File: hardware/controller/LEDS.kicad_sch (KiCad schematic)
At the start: 19 parts, among them IC901 PCA9685PW_Q900,118, Q901 IRLML6402TRPBF, Q902 IRLML6402TRPBF

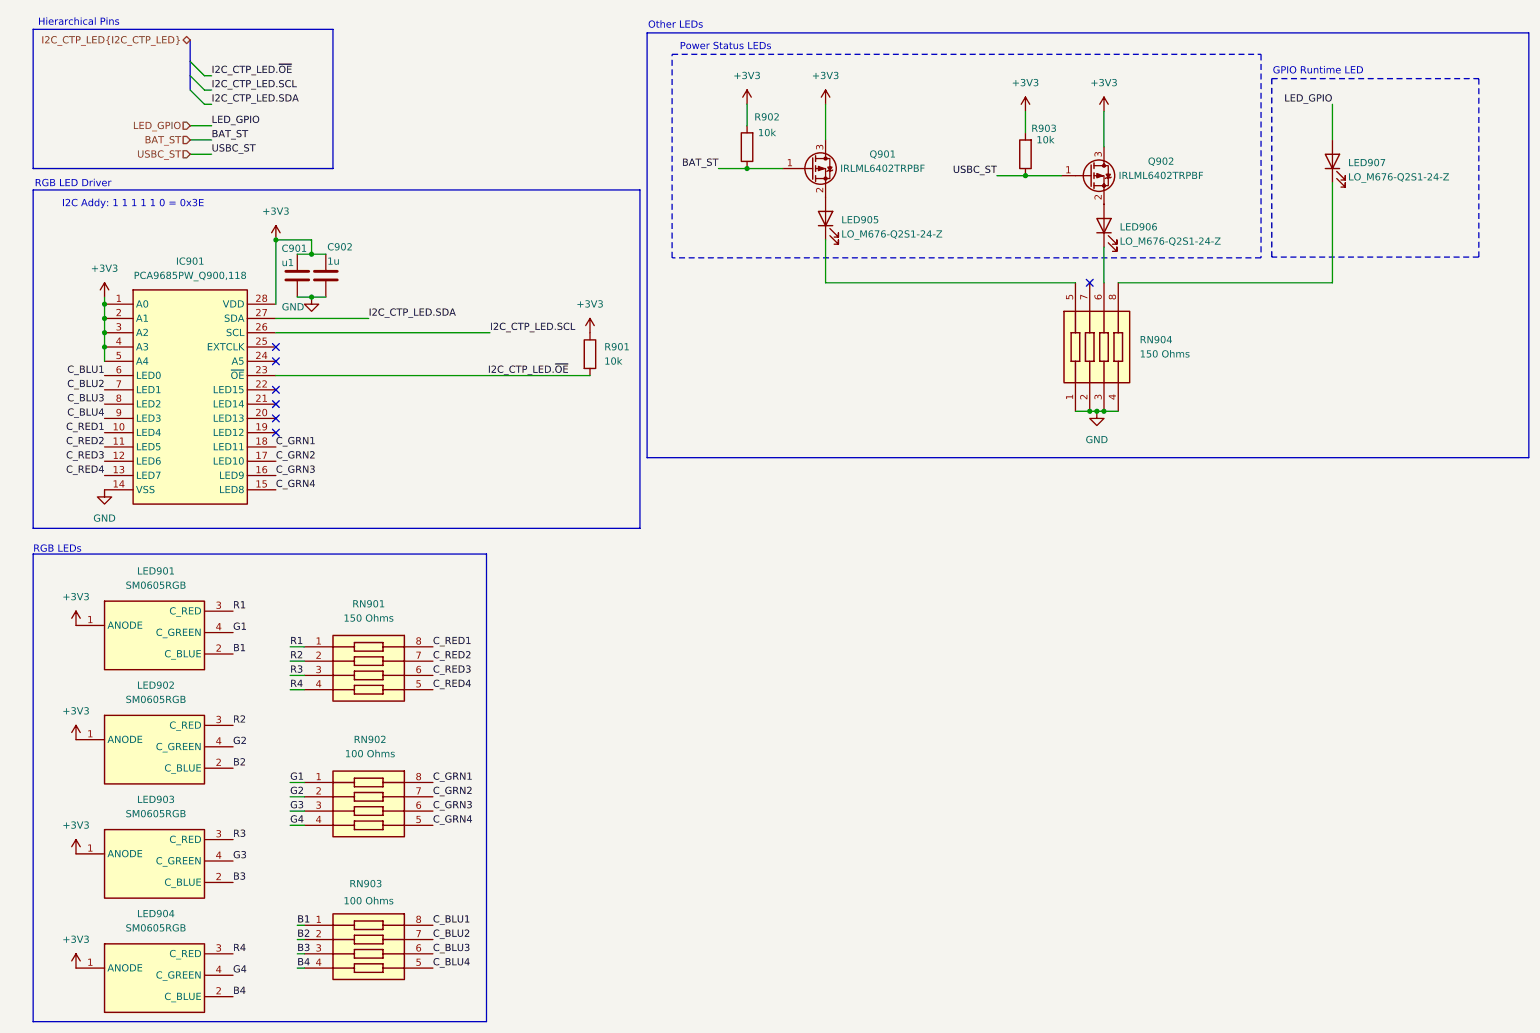
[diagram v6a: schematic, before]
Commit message: save before axing motor driver ic's
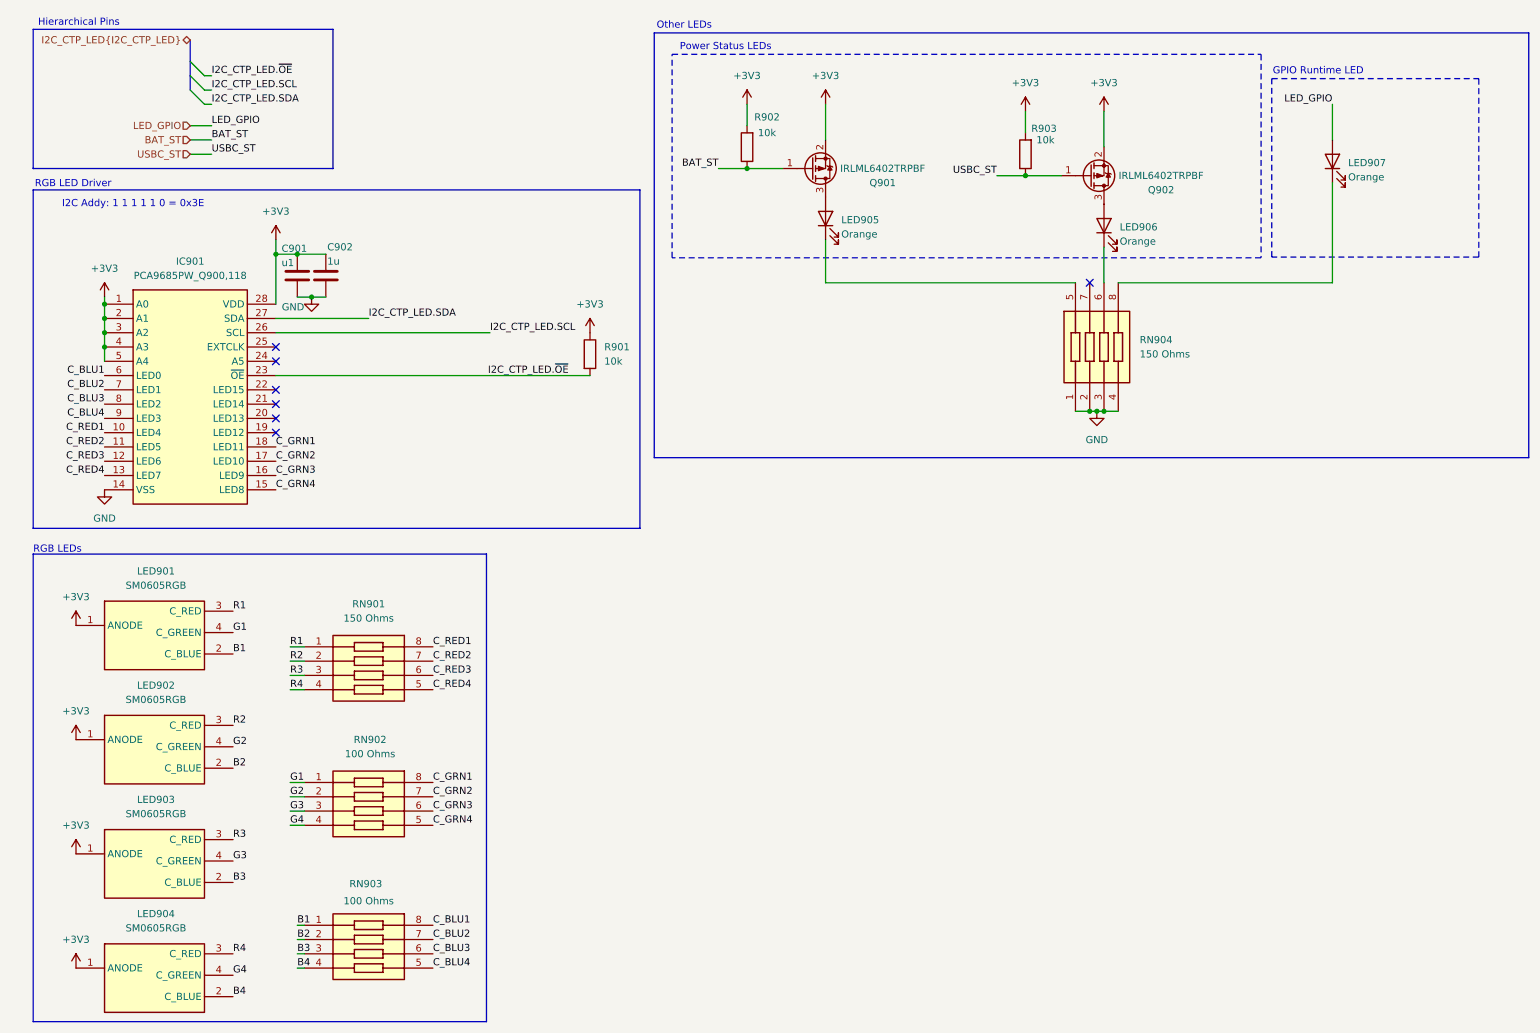
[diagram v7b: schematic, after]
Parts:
- LED905, LED906, LED907: value LO_M676-Q2S1-24-Z -> Orange
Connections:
- net +3V3: now also Q901.2 (S), Q902.2 (S); no longer Q901.3 (D), Q902.3 (D)
- net at LED906.2 (A): now also Q902.3 (D); no longer Q902.2 (S)
- net at LED905.2 (A): now also Q901.3 (D); no longer Q901.2 (S)
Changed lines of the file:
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@@
 	(paper "A4")
 	(rectangle
-		(start 124.46 17.78)
+		(start 125.73 17.78)
 		(end 281.305 93.345)
 		(stroke
@@
 	(text "Other LEDs"
 		(exclude_from_sim no)
-		(at 129.54 16.51 0)
+		(at 131.064 16.51 0)
 		(effects
 			(font
@@
 	)
 	(junction
-		(at 58.42 54.61)
+		(at 62.23 57.15)
 		(diameter 0)
 		(color 0 0 0 0)
@@
 	)
 	(junction
-		(at 64.77 57.15)
+		(at 142.24 41.91)
 		(diameter 0)
 		(color 0 0 0 0)
 	)
 	(junction
-		(at 142.24 41.91)
+		(at 27.94 66.04)
 		(diameter 0)
 		(color 0 0 0 0)
 	)
 	(junction
-		(at 27.94 66.04)
+		(at 58.42 57.15)
 		(diameter 0)
 		(color 0 0 0 0)
@@
 	(wire
 		(pts
+			(xy 58.42 57.15) (xy 58.42 66.04)
+		)
+		(stroke
+			(width 0)
+			(type default)
+		)
+	)
+	(wire
+		(pts
 			(xy 191.77 31.75) (xy 191.77 35.56)
 		)
@@
 	(wire
 		(pts
-			(xy 58.42 54.61) (xy 58.42 66.04)
+			(xy 58.42 54.61) (xy 58.42 57.15)
 		)
 		(stroke
@@
 	(wire
 		(pts
-			(xy 58.42 54.61) (xy 64.77 54.61)
+			(xy 58.42 57.15) (xy 62.23 57.15)
 		)
 		(stroke
@@
 	(wire
 		(pts
-			(xy 62.23 57.15) (xy 64.77 57.15)
-		)
-		(stroke
-			(width 0)
-			(type default)
-		)
-	)
-	(wire
-		(pts
-			(xy 64.77 57.15) (xy 67.31 57.15)
+			(xy 62.23 57.15) (xy 67.31 57.15)
 		)
 		(stroke
@@
 	(wire
 		(pts
-			(xy 64.77 54.61) (xy 64.77 57.15)
-		)
-		(stroke
-			(width 0)
-			(type default)
-		)
-	)
-	(wire
-		(pts
 			(xy 45.72 27.94) (xy 46.99 27.94)
 		)
@@
 		(lib_id "Transistor_FET:IRLML6402")
 		(at 203.2 43.18 0)
+		(mirror x)
 		(unit 1)
 		(exclude_from_sim no)
@@
 		(dnp no)
 		(property "Reference" "Q902"
-			(at 215.9 40.64 0)
+			(at 215.9 45.72 0)
 			(effects
 				(font
@@
 		)
 		(property "Footprint" "Package_TO_SOT_SMD:SOT-23"
-			(at 208.28 45.085 0)
+			(at 208.28 41.275 0)
 			(effects
 				(font
@@
 		)
 		(property "Datasheet" "https://www.infineon.com/dgdl/irlml6402pbf.pdf?fileId=5546d462533600a401535668d5c2263c"
-			(at 208.28 46.99 0)
+			(at 208.28 39.37 0)
 			(effects
 				(font
@@
 			)
 		)
-		(property "Value" "LO_M676-Q2S1-24-Z"
+		(property "Value" "Orange"
 			(at 249.174 43.434 90)
 			(effects
@@
 			)
 		)
-		(property "Value" "LO_M676-Q2S1-24-Z"
+		(property "Value" "Orange"
 			(at 208.534 54.864 90)
 			(effects
@@
 		(lib_id "Transistor_FET:IRLML6402")
 		(at 153.67 41.91 0)
+		(mirror x)
 		(unit 1)
 		(exclude_from_sim no)
@@
 		(dnp no)
 		(property "Reference" "Q901"
-			(at 166.37 39.37 0)
+			(at 166.37 44.45 0)
 			(effects
 				(font
@@
 		)
 		(property "Footprint" "Package_TO_SOT_SMD:SOT-23"
-			(at 158.75 43.815 0)
+			(at 158.75 40.005 0)
 			(effects
 				(font
@@
 		)
 		(property "Datasheet" "https://www.infineon.com/dgdl/irlml6402pbf.pdf?fileId=5546d462533600a401535668d5c2263c"
-			(at 158.75 45.72 0)
+			(at 158.75 38.1 0)
 			(effects
 				(font
@@
 			)
 		)
-		(property "Value" "LO_M676-Q2S1-24-Z"
+		(property "Value" "Orange"
 			(at 159.004 53.594 90)
 			(effects
